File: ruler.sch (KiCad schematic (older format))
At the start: 1 part, among them J1 Conn_01x01

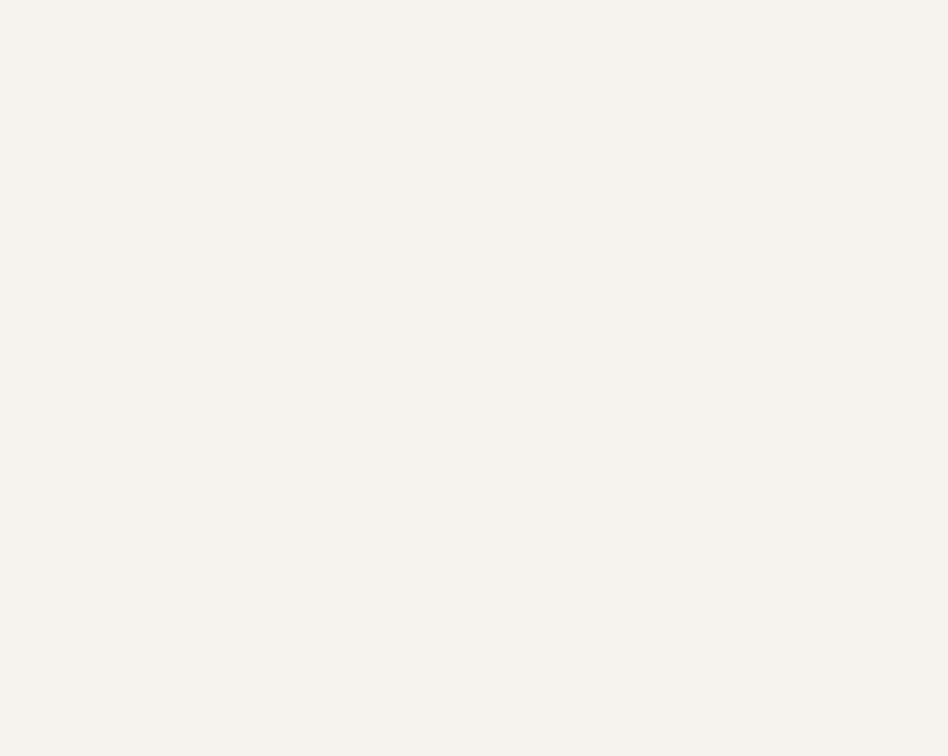
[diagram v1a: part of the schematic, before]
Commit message: Add some push-buttons and LEDs to schematic
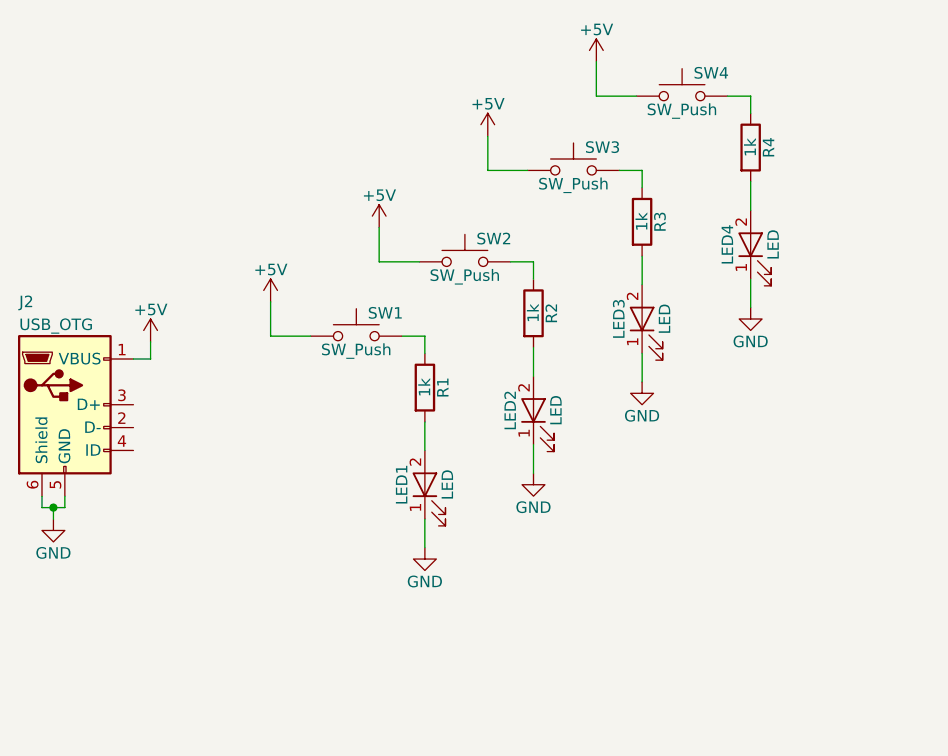
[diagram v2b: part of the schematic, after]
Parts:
- added J2: USB_OTG, symbol USB_OTG
- added LED1: LED, KiCad/LEDs.pretty:LED_0402, symbol LED
- added LED2: LED, KiCad/LEDs.pretty:LED_0603, symbol LED
- added LED3: LED, KiCad/LEDs.pretty:LED_0805, symbol LED
- added LED4: LED, KiCad/LEDs.pretty:LED_1206, symbol LED
- added R1: 1k, KiCad/Resistors_SMD.pretty:R_0402, symbol R
- added R2: 1k, KiCad/Resistors_SMD.pretty:R_0603, symbol R
- added R3: 1k, KiCad/Resistors_SMD.pretty:R_0805, symbol R
- added R4: 1k, KiCad/Resistors_SMD.pretty:R_1206, symbol R
- added SW1, SW2, SW3, SW4: SW_Push, symbol SW_Push
- J1: footprint custom:pcbart -> drawing:drawing
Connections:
- new net: R1.1, SW1.2
- new net: LED1.2 (A), R1.2
- new net: R2.1, SW2.2
- new net: LED2.2 (A), R2.2
- new net: R3.1, SW3.2
- new net: LED3.2 (A), R3.2
- new net: R4.1, SW4.2
- new net: LED4.2 (A), R4.2
- new net +5V: J2.1 (VBUS), SW1.1, SW2.1, SW3.1, SW4.1
- new net GND: J2.5 (GND), J2.6 (Shield), LED1.1 (K), LED2.1 (K), LED3.1 (K), LED4.1 (K)

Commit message: Do some layouting
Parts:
- added LED1: LED TEST PADS, custom:led_test_pads, symbol device:LED
- added R_201: 1k, KiCad/Resistors_SMD.pretty:R_0201, symbol device:R
- added SW5: SW_DPDT_x2, digikey/digikey-kicad-library/digikey-footprints.pretty:Switch_Slide_JS202011SCQN, symbol Switch:SW_DPDT_x2
- J1: symbol Conn_01x01 -> conn:Conn_01x01
- J2: footprint (none) -> smisioto.eu/kicad_libs/modules/w_conn_pc.pretty:conn_usb_B_micro_smd; symbol USB_OTG -> conn:USB_OTG
- LED2: renamed from LED1; value LED -> 0402; symbol LED -> device:LED
- LED3: renamed from LED2; value LED -> 0603; symbol LED -> device:LED
- LED4: renamed from LED3; value LED -> 0805; symbol LED -> device:LED
- LED5: renamed from LED4; value LED -> 1206; symbol LED -> device:LED
- R_1206: renamed from R4; symbol R -> device:R
- R_402: renamed from R1; symbol R -> device:R
- R_603: renamed from R2; symbol R -> device:R
- R_805: renamed from R3; symbol R -> device:R
- SW1: value SW_Push -> 6x6mm; footprint (none) -> digikey/digikey-kicad-library/digikey-footprints.pretty:Switch_Tactile_6x6mm_Vertical_SMD; symbol SW_Push -> switches:SW_Push
- SW2: footprint (none) -> smisioto.eu/kicad_libs/modules/w_switch.pretty:smd_push2; symbol SW_Push -> switches:SW_Push
- SW3: footprint (none) -> smisioto.eu/kicad_libs/modules/w_switch.pretty:smd_push; symbol SW_Push -> switches:SW_Push
- SW4: value SW_Push -> B3U-1000P; footprint (none) -> digikey/digikey-kicad-library/digikey-footprints.pretty:Switch_Tactile_SMD_B3U-1000P; symbol SW_Push -> switches:SW_Push
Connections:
- net labels added: LED_V+, SW_V+
- wire segments 30 -> 44
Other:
- moved on the sheet: LED2, LED4, LED5, R_1206, R_402, R_805, SW1, SW2, SW3, SW4

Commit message: Add more push-buttons
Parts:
- added SW6: 6x6mm, custom:FSM2JSMA, symbol switches:SW_Push
- added SW7: 6x6mm, KiCad/Buttons_Switches_SMD.pretty:SW_SPST_KMR2, symbol switches:SW_Push
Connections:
- wire segments 44 -> 55
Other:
- moved on the sheet: SW3
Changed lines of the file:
@@
 	3000 2475 3000 2350
 Wire Wire Line
-	2075 1825 2075 1975
-Wire Wire Line
 	2075 1975 2400 1975
 Wire Wire Line
-	2800 1975 3000 1975
+	2800 1975 2875 1975
 Wire Wire Line
 	3000 1975 3000 2050
@@
 L switches:SW_Push SW3
 U 1 1 5AF1BC93
-P 3300 1575
-F 0 "SW3" H 3350 1675 50  0000 L CNN
-F 1 "SW_Push" H 3300 1515 50  0000 C CNN
-F 2 "smisioto.eu/kicad_libs/modules/w_switch.pretty:smd_push" H 3300 1775 50  0001 C CNN
-F 3 "" H 3300 1775 50  0001 C CNN
-	1    3300 1575
+P 2600 1725
+F 0 "SW3" H 2650 1825 50  0000 L CNN
+F 1 "SW_Push" H 2600 1665 50  0000 C CNN
+F 2 "smisioto.eu/kicad_libs/modules/w_switch.pretty:smd_push" H 2600 1925 50  0001 C CNN
+F 3 "" H 2600 1925 50  0001 C CNN
+	1    2600 1725
 	1    0    0    -1
 $EndComp
@@
 LED_V+
 Wire Wire Line
-	4400 1025 4400 1250
+	4400 1025 4400 1100
 Connection ~ 4400 1250
 Text GLabel 2950 1425 0    50   Input ~ 0
@@
 Text GLabel 3600 1525 1    50   Input ~ 0
 LED_V+
-Text GLabel 2075 1825 0    50   Input ~ 0
+Text GLabel 2025 1825 0    50   Input ~ 0
 SW_V+
 Text GLabel 3000 1950 1    50   Input ~ 0
@@
 	3600 1525 3600 1575
 Connection ~ 3600 1575
+$Comp
+L switches:SW_Push SW6
+U 1 1 5AF214E5
+P 3300 1575
+F 0 "SW6" H 3075 1775 50  0000 L CNN
+F 1 "6x6mm" H 3300 1515 50  0000 C CNN
+F 2 "custom:FSM2JSMA" H 3300 1775 50  0001 C CNN
+F 3 "" H 3300 1775 50  0001 C CNN
+	1    3300 1575
+	1    0    0    -1
+$EndComp
+$Comp
+L switches:SW_Push SW7
+U 1 1 5AF21638
+P 4100 900
+F 0 "SW7" H 3875 1100 50  0000 L CNN
+F 1 "6x6mm" H 4100 840 50  0000 C CNN
+F 2 "KiCad/Buttons_Switches_SMD.pretty:SW_SPST_KMR2" H 4100 1100 50  0001 C CNN
+F 3 "" H 4100 1100 50  0001 C CNN
+	1    4100 900
+	1    0    0    -1
+$EndComp
+Wire Wire Line
+	3900 900  3725 900
+Wire Wire Line
+	3725 900  3725 1000
+Connection ~ 3725 1000
+Wire Wire Line
+	4300 900  4300 1100
+Wire Wire Line
+	4300 1100 4400 1100
+Connection ~ 4400 1100
+Wire Wire Line
+	4400 1100 4400 1250
+Wire Wire Line
+	2400 1725 2075 1725
+Wire Wire Line
+	2075 1725 2075 1825
+Wire Wire Line
+	2025 1825 2075 1825
+Connection ~ 2075 1825
+Wire Wire Line
+	2075 1825 2075 1975
+Wire Wire Line
+	2800 1725 2875 1725
+Wire Wire Line
+	2875 1725 2875 1975
+Connection ~ 2875 1975
+Wire Wire Line
+	2875 1975 3000 1975
 $EndSCHEMATC

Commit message: Re-enable switching individual LEDs on
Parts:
- added R_? (x4): 1k, KiCad/Resistors_SMD.pretty:R_1206, symbol device:R
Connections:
- wire segments 55 -> 67
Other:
- moved on the sheet: LED2, LED3, LED4, LED5, R_1206, R_402, R_603, R_805, SW1, SW2, SW3, SW4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

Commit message: Add bigger resistors
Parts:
- R3: renamed from R_?; footprint KiCad/Resistors_SMD.pretty:R_1206 -> KiCad/Resistors_SMD.pretty:R_1210
- R5: renamed from R_?; footprint KiCad/Resistors_SMD.pretty:R_1206 -> KiCad/Resistors_SMD.pretty:R_1218
- R7: renamed from R_?; footprint KiCad/Resistors_SMD.pretty:R_1206 -> KiCad/Resistors_SMD.pretty:R_2010
- R9: renamed from R_?; footprint KiCad/Resistors_SMD.pretty:R_1206 -> KiCad/Resistors_SMD.pretty:R_2512
- SW1: renamed from SW7; value 6x6mm -> KMR2
- SW5: renamed from SW6; value 6x6mm -> FSM2JSMA
- renumbered J2 to J1, J1 to J2, R_201 to R1, R_402 to R2, R_603 to R4, R_805 to R6, R_1206 to R8, SW4 to SW2, SW2 to SW4, SW1 to SW6, SW5 to SW7
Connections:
- wire segments 67 -> 66
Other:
- moved on the sheet: LED1, LED2, LED3, LED4, LED5, R1, R2, R3, R4, R5, R6, R7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

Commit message: Add diodes
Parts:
- removed R3: 1k, KiCad/Resistors_SMD.pretty:R_1210, symbol device:R
- removed R5: 1k, KiCad/Resistors_SMD.pretty:R_1218, symbol device:R
- removed R7: 1k, KiCad/Resistors_SMD.pretty:R_2010, symbol device:R
- removed R9: 1k, KiCad/Resistors_SMD.pretty:R_2512, symbol device:R
- added D1: SMA, KiCad/Diodes_SMD.pretty:D_SMA, symbol device:D
- added D2: SMB, KiCad/Diodes_SMD.pretty:D_SMB, symbol device:D
- added D3: SMC, KiCad/Diodes_SMD.pretty:D_SMC, symbol device:D
- added D4: SOD-123, KiCad/Diodes_SMD.pretty:D_SOD-123, symbol device:D
- added D5: SOD-323, KiCad/Diodes_SMD.pretty:D_SOD-323, symbol device:D
- added D6: SOD-523, KiCad/Diodes_SMD.pretty:D_SOD-523, symbol device:D
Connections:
- wire segments 66 -> 62
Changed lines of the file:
@@
 	4025 5100 4025 5225
-Wire Wire Line
-	4025 4800 4025 4750
 Wire Wire Line
 	3925 4300 3950 4300
@@
 	5900 5125 5900 5250
 Wire Wire Line
-	5900 4825 5900 4775
-Wire Wire Line
 	4975 4325 5300 4325
 Wire Wire Line
@@
 	7475 5050 7475 5175
 Wire Wire Line
-	7475 4750 7475 4700
-Wire Wire Line
 	6825 4100 6825 4250
 Wire Wire Line
@@
 	9250 5200 9250 5325
 Wire Wire Line
-	9250 4900 9250 4825
-Wire Wire Line
 	8575 4400 8750 4400
 Wire Wire Line
@@
 Wire Wire Line
 	8575 4150 8575 4400
-Text GLabel 9825 4350 1    50   Input ~ 0
-LED_V+
 Text GLabel 6825 4100 0    50   Input ~ 0
 SW_V+
@@
 Wire Wire Line
 	5775 4325 5900 4325
-$Comp
-L device:R R9
-U 1 1 5AF2AF93
-P 9825 4650
-F 0 "R9" V 9905 4650 50  0000 C CNN
-F 1 "1k" V 9825 4650 50  0000 C CNN
-F 2 "KiCad/Resistors_SMD.pretty:R_2512" V 9755 4650 50  0001 C CNN
-F 3 "" H 9825 4650 50  0001 C CNN
-	1    9825 4650
-	1    0    0    -1
-$EndComp
-Wire Wire Line
-	9825 4350 9825 4500
-Wire Wire Line
-	9825 4800 9825 4825
-Wire Wire Line
-	9825 4825 9250 4825
-Connection ~ 9250 4825
-Wire Wire Line
-	9250 4825 9250 4775
-Text GLabel 8050 4225 1    50   Input ~ 0
+Text GLabel 4175 3775 1    50   Input ~ 0
 LED_V+
-$Comp
-L device:R R7
-U 1 1 5AF2CC92
-P 8050 4525
-F 0 "R7" V 8130 4525 50  0000 C CNN
-F 1 "1k" V 8050 4525 50  0000 C CNN
-F 2 "KiCad/Resistors_SMD.pretty:R_2010" V 7980 4525 50  0001 C CNN
-F 3 "" H 8050 4525 50  0001 C CNN
-	1    8050 4525
-	1    0    0    -1
-$EndComp
-Wire Wire Line
-	8050 4225 8050 4375
-Wire Wire Line
-	8050 4675 8050 4700
-Wire Wire Line
-	8050 4700 7475 4700
-Connection ~ 7475 4700
-Wire Wire Line
-	7475 4700 7475 4625
-Text GLabel 6450 4300 1    50   Input ~ 0
-LED_V+
-$Comp
-L device:R R5
-U 1 1 5AF2DBAE
-P 6450 4600
-F 0 "R5" V 6530 4600 50  0000 C CNN
-F 1 "1k" V 6450 4600 50  0000 C CNN
-F 2 "KiCad/Resistors_SMD.pretty:R_1218" V 6380 4600 50  0001 C CNN
-F 3 "" H 6450 4600 50  0001 C CNN
-	1    6450 4600
-	1    0    0    -1
-$EndComp
-Wire Wire Line
-	6450 4300 6450 4450
-Wire Wire Line
-	6450 4750 6450 4775
-Wire Wire Line
-	5900 4775 6450 4775
-Connection ~ 5900 4775
-Wire Wire Line
-	5900 4775 5900 4700
-Text GLabel 4400 4275 1    50   Input ~ 0
-LED_V+
-$Comp
-L device:R R3
-U 1 1 5AF2FE68
-P 4400 4575
-F 0 "R3" V 4480 4575 50  0000 C CNN
-F 1 "1k" V 4400 4575 50  0000 C CNN
-F 2 "KiCad/Resistors_SMD.pretty:R_1210" V 4330 4575 50  0001 C CNN
-F 3 "" H 4400 4575 50  0001 C CNN
-	1    4400 4575
-	1    0    0    -1
-$EndComp
-Wire Wire Line
-	4400 4275 4400 4425
-Wire Wire Line
-	4400 4725 4400 4750
-Wire Wire Line
-	4025 4750 4400 4750
-Connection ~ 4025 4750
-Wire Wire Line
-	4025 4750 4025 4675
 Wire Wire Line
 	3525 3950 3525 4300
@@
 Wire Wire Line
 	3950 4300 4025 4300
+$Comp
+L device:D D1
+U 1 1 5AF423A2
+P 4175 4125
+F 0 "D1" V 4221 4046 50  0000 R CNN
+F 1 "SMA" V 4130 4046 50  0000 R CNN
+F 2 "KiCad/Diodes_SMD.pretty:D_SMA" H 4175 4125 50  0001 C CNN
+F 3 "" H 4175 4125 50  0001 C CNN
+	1    4175 4125
+	0    -1   -1   0
+$EndComp
+Wire Wire Line
+	4175 3775 4175 3975
+Wire Wire Line
+	4175 4275 4175 4300
+Wire Wire Line
+	4175 4300 4025 4300
+Connection ~ 4025 4300
+Wire Wire Line
+	4025 4675 4025 4800
+Wire Wire Line
+	5900 4700 5900 4825
+Text GLabel 6050 3800 1    50   Input ~ 0
+LED_V+
+$Comp
+L device:D D2
+U 1 1 5AF48CEA
+P 6050 4150
+F 0 "D2" V 6096 4071 50  0000 R CNN
+F 1 "SMB" V 6005 4071 50  0000 R CNN
+F 2 "KiCad/Diodes_SMD.pretty:D_SMB" H 6050 4150 50  0001 C CNN
+F 3 "" H 6050 4150 50  0001 C CNN
+	1    6050 4150
+	0    -1   -1   0
+$EndComp
+Wire Wire Line
+	6050 3800 6050 4000
+Wire Wire Line
+	6050 4300 6050 4325
+Wire Wire Line
+	6050 4325 5900 4325
+Connection ~ 5900 4325
+Text GLabel 7625 3725 1    50   Input ~ 0
+LED_V+
+$Comp
+L device:D D3
+U 1 1 5AF49F44
+P 7625 4075
+F 0 "D3" V 7671 3996 50  0000 R CNN
+F 1 "SMC" V 7580 3996 50  0000 R CNN
+F 2 "KiCad/Diodes_SMD.pretty:D_SMC" H 7625 4075 50  0001 C CNN
+F 3 "" H 7625 4075 50  0001 C CNN
+	1    7625 4075
+	0    -1   -1   0
+$EndComp
+Wire Wire Line
+	7625 3725 7625 3925
+Wire Wire Line
+	7625 4225 7625 4250
+Wire Wire Line
+	7625 4250 7475 4250
+Connection ~ 7475 4250
+Text GLabel 9400 3875 1    50   Input ~ 0
+LED_V+
+$Comp
+L device:D D4
+U 1 1 5AF4B2D9
+P 9400 4225
+F 0 "D4" V 9446 4146 50  0000 R CNN
+F 1 "SOD-123" V 9355 4146 50  0000 R CNN
+F 2 "KiCad/Diodes_SMD.pretty:D_SOD-123" H 9400 4225 50  0001 C CNN
+F 3 "" H 9400 4225 50  0001 C CNN
+	1    9400 4225
+	0    -1   -1   0
+$EndComp
+Wire Wire Line
+	9400 3875 9400 4075
+Wire Wire Line
+	9400 4375 9400 4400
+Wire Wire Line
+	9400 4400 9250 4400
+Connection ~ 9250 4400
+Wire Wire Line
+	9250 4775 9250 4900
+$Comp
+L device:D D5
+U 1 1 5AF4E276
+P 9950 4225
+F 0 "D5" V 9996 4146 50  0000 R CNN
+F 1 "SOD-323" V 9905 4146 50  0000 R CNN
+F 2 "KiCad/Diodes_SMD.pretty:D_SOD-323" H 9950 4225 50  0001 C CNN
+F 3 "" H 9950 4225 50  0001 C CNN
+	1    9950 4225
+	0    -1   -1   0
+$EndComp
+$Comp
+L device:D D6
+U 1 1 5AF4E2E0
+P 10550 4200
+F 0 "D6" V 10596 4121 50  0000 R CNN
+F 1 "SOD-523" V 10505 4121 50  0000 R CNN
+F 2 "KiCad/Diodes_SMD.pretty:D_SOD-523" H 10550 4200 50  0001 C CNN
+F 3 "" H 10550 4200 50  0001 C CNN
+	1    10550 4200
+	0    -1   -1   0
+$EndComp
+Wire Wire Line
+	7475 4625 7475 4750
 $EndSCHEMATC

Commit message: Delete all routing and re-arrange
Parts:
- SW7: value SW_DPDT_x2 -> JS202011SCQN
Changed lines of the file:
@@
 P 10725 2500
 F 0 "SW7" H 10725 2785 50  0000 C CNN
-F 1 "SW_DPDT_x2" H 10725 2694 50  0000 C CNN
+F 1 "JS202011SCQN" H 10725 2694 50  0000 C CNN
 F 2 "digikey/digikey-kicad-library/digikey-footprints.pretty:Switch_Slide_JS202011SCQN" H 10725 2500 50  0001 C CNN
 F 3 "" H 10725 2500 50  0001 C CNN
@@
 P 10775 3150
 F 0 "SW7" H 10775 3435 50  0000 C CNN
-F 1 "SW_DPDT_x2" H 10775 3344 50  0000 C CNN
+F 1 "JS202011SCQN" H 10775 3344 50  0000 C CNN
 F 2 "digikey/digikey-kicad-library/digikey-footprints.pretty:Switch_Slide_JS202011SCQN" H 10775 3150 50  0001 C CNN
 F 3 "" H 10775 3150 50  0001 C CNN
